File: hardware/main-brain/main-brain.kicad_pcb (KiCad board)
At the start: 2 copper layers, 170 x 100 mm, 35 parts, among them J1 19V, J2 CAN+5V, J3 19V OUT, J4 I2S OUT, Q1 AO3481, Q2 2N7000, U1 SN65HVD230

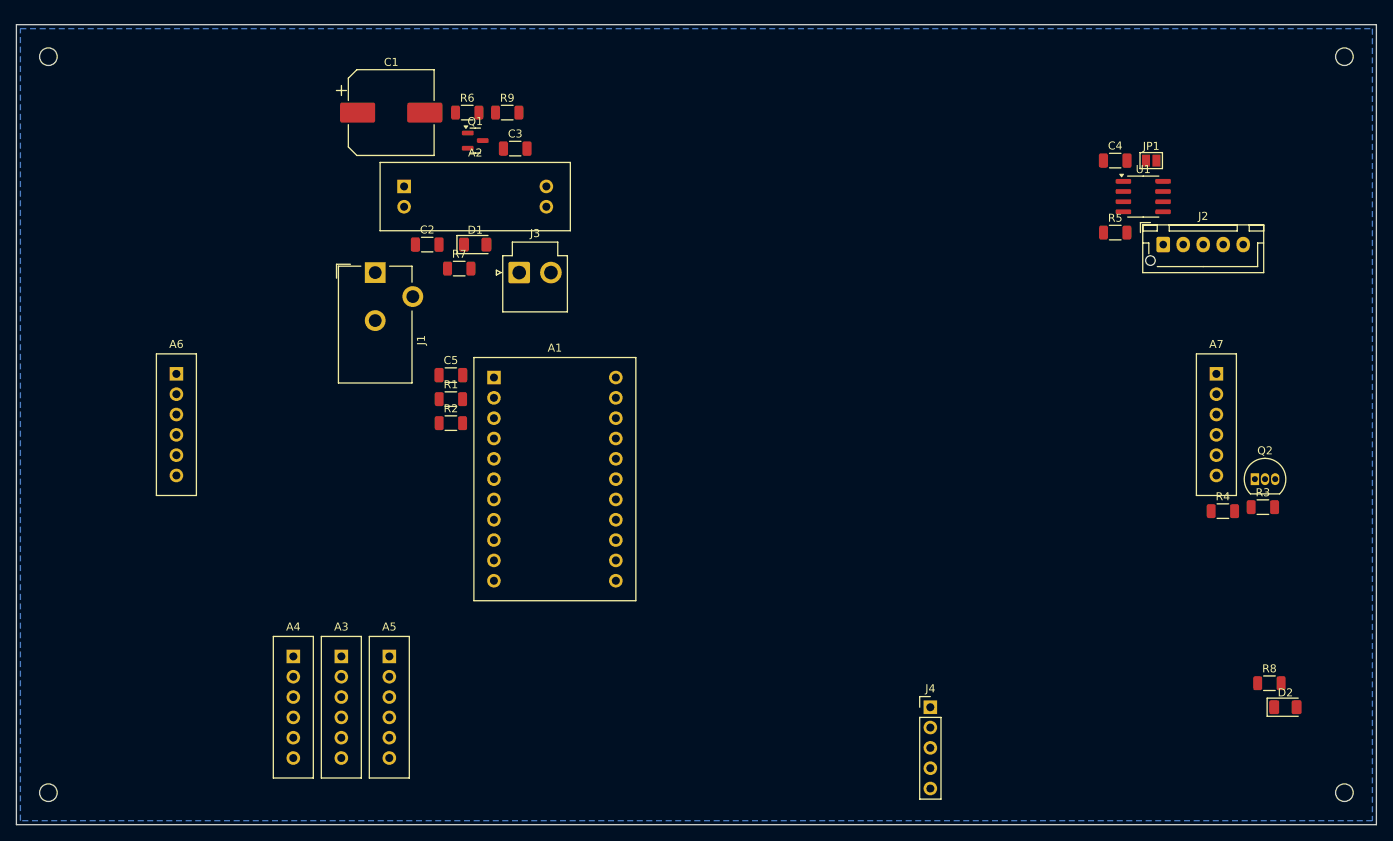
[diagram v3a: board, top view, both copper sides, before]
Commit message: Use an AO3400A in SOT-23 for the kill line
The kill-line FET was specified as a 2N7000 in TO-92, which is not a part on
hand. The AO3400A is: single N-channel, SOT-23, Vgs(th) 0.7 V so it is fully
enhanced by a 3.3 V GPIO, and 30 mOhm where the job asks for roughly 120 mA of
sink. KiCad carries the symbol natively with the SOT-23 G/S/D pinout, and it is
the same family, package and pinout as the AO3401A already used for the
reverse-polarity FET.

A dual N-channel in SC-88/SOT-363 was the alternative and works electrically -
Vgs(th) 1.2 V max, 250 mA, 1 Ohm - but it puts a 0.65 mm pitch six-pin part on a
board meant to be hand-soldered and leaves half a device needing its gate tied
off. The single in SOT-23 is the better fit for the same job.

Co-Authored-By: Claude Opus 5 <noreply@anthropic.com>
Claude-Session: https://claude.ai/code/session_011qFNDvbo1RnNn3sy9mr9bh
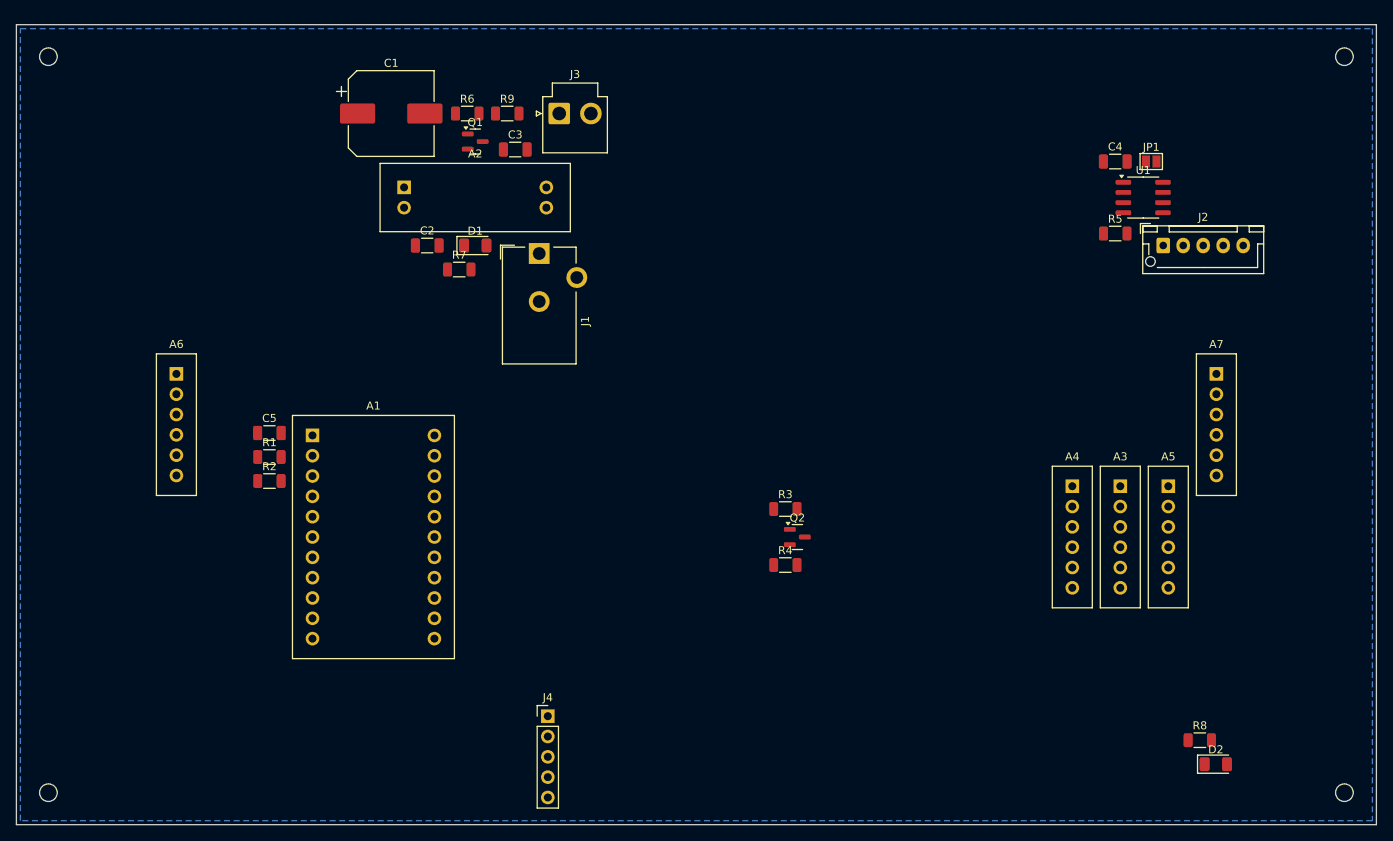
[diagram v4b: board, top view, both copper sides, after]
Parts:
- Q2: value 2N7000 -> AO3400A; footprint Package_TO_SOT_THT:TO-92_Inline -> Package_TO_SOT_SMD:SOT-23
- moved A3 99.7 mm to (138.0, 64.0)
- moved A4 99.7 mm to (132.0, 64.0)
- moved A5 99.7 mm to (144.0, 64.0)
- moved R3 59.7 mm to (96.1, 60.5)
- moved Q2 57.6 mm to (97.6, 64.0)
- moved R4 55.1 mm to (96.1, 67.5)
- moved J4 47.8 mm to (66.4, 86.4)
- moved C5 23.8 mm to (31.6, 51.0)
- moved R1 23.8 mm to (31.6, 54.0)
- moved R2 23.8 mm to (31.6, 57.0)
- moved A1 23.8 mm to (44.6, 64.0)
- moved J1 20.6 mm to (65.4, 28.6)
- moved J3 20.5 mm to (67.9, 11.1)
- moved D2 11.2 mm to (149.9, 92.4)
- moved R8 11.2 mm to (147.9, 89.4)
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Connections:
- Q2 pad 1: GND -> KILL_GATE
- Q2 pad 2: KILL_GATE -> GND

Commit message: Lay the node out around right-angle connectors, and spec what it can do
The connector order is all right-angle JST: 3-pin XH, 5-pin XH and 2-pin VH,
with no 2-pin XH at all. A right-angle body opens toward +Y at 0 degrees, so
the rotation is what points a cable off the board, and the placer had no
concept of rotation - it put J2 through the crystal and pushed J1 and J7 past
the outline.

kigen.rotate_boxes turns a footprint's courtyard with it; pinned entries now
take an optional third element; check.py rotates the library courtyard before
testing overlap and outline, and verifies the angle as well as the position.

Floorplan, following the three placement rules:
  - CAN on opposite edges, J2 left and J3 right
  - the whole motor loom on the bottom edge: phases, NTC, encoder, SPI
  - power and SWD on the top
All eight ports are on the perimeter, none closer than 1.1 mm to an edge.

Four things the auto-placer got wrong and are now pinned:
  - U6 sat under the driver module, stacking the LDO's heat under the bridge's
  - R7 sat on A1's exact origin; it belongs under the module, but deliberately
    placed clear of every pad rather than by accident
  - both crystal load caps sat at one end of a 20 mm hand-solder footprint,
    leaving one of them 22 mm from its terminal
  - the node-ID pull-ups were stranded 13 mm from their jumpers

Vbus divider R4 4k7 -> 10k. 100 k / 4k7 read 19 V as 0.85 V, a quarter of the
ADC span. 100 k / 10 k reads 1.73 V and clips at 36 V.

Two renderer bugs, both only visible once something was rotated or mirrored:
  - pad angles were being summed with the footprint angle, but KiCad stores a
    pad's angle absolutely
  - the mirror reflected about the origin rather than the view box, and the
    substrate rect took its min in board space instead of screen space, so the
    bottom view sat 13 mm left and grew a slab off the far edge

New docs:
  - docs/capabilities.md - bus range, torque and current resolution, loop
    rates, CAN bandwidth a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
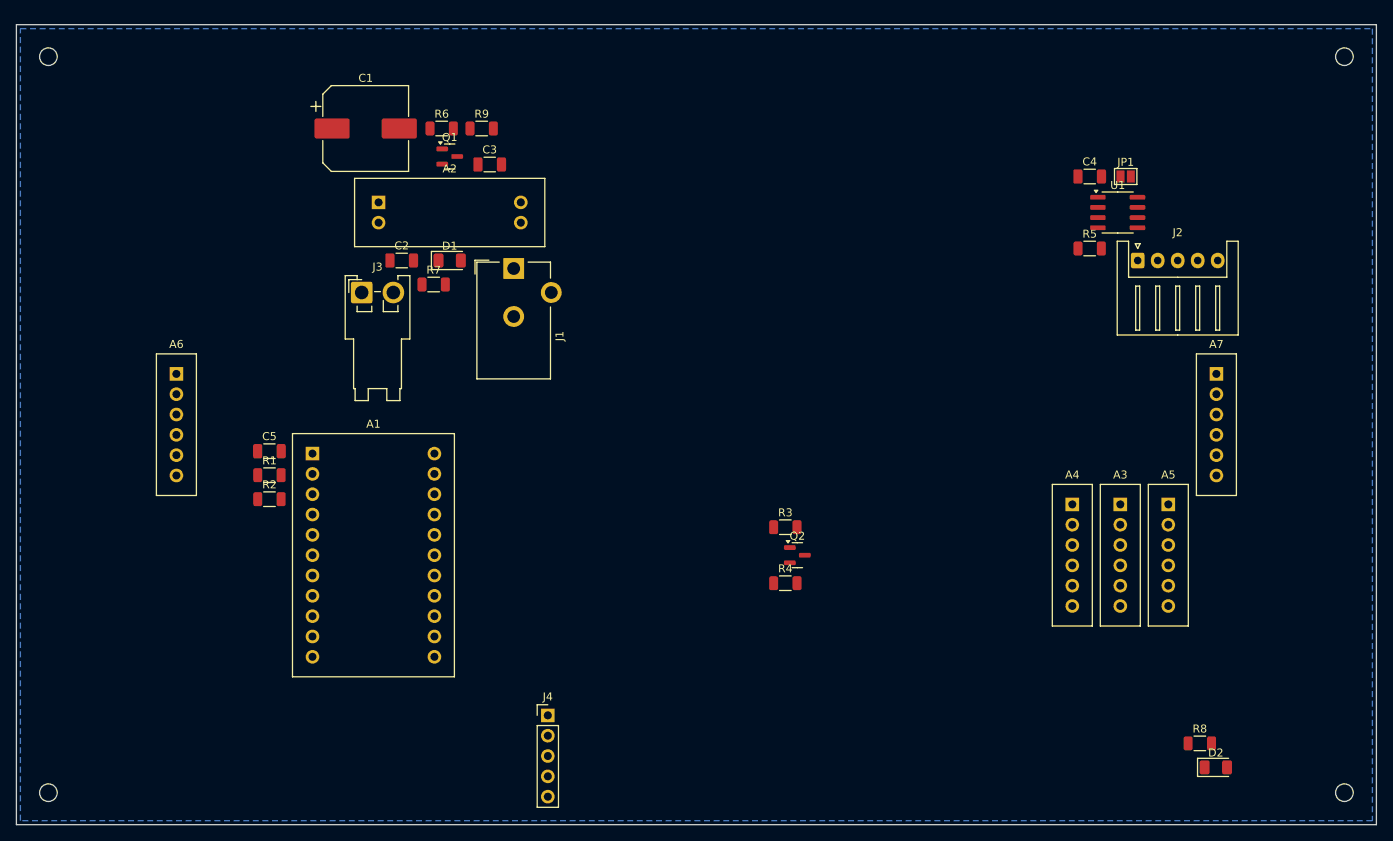
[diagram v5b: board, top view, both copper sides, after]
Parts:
- J2: footprint Connector_JST:JST_XH_B5B-XH-AM_1x05_P2.50mm_Vertical -> Connector_JST:JST_XH_S5B-XH-A_1x05_P2.50mm_Horizontal
- J3: footprint Connector_JST:JST_VH_B2P-VH_1x02_P3.96mm_Vertical -> Connector_JST:JST_VH_S2P-VH_1x02_P3.96mm_Horizontal
- moved J3 33.3 mm to (43.2, 33.5)
- moved C4 3.70 mm to (134.2, 19.0)
- moved J2 3.70 mm to (140.2, 29.5)
- moved JP1 3.70 mm to (138.7, 19.0)
- moved R5 3.70 mm to (134.2, 28.0)
- moved U1 3.70 mm to (137.7, 23.5)
- moved A2 3.70 mm to (54.2, 23.5)
- moved C1 3.70 mm to (43.7, 13.0)
- moved C2 3.70 mm to (48.2, 29.5)
- moved C3 3.70 mm to (59.2, 17.5)
- moved D1 3.70 mm to (54.2, 29.5)
- moved Q1 3.70 mm to (54.2, 16.5)
- moved R6 3.70 mm to (53.2, 13.0)
- moved R7 3.70 mm to (52.2, 32.5)
- moved R9 3.70 mm to (58.2, 13.0)
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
